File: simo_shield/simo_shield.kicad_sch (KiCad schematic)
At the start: 3 parts, among them U1 YAAJ_BluePill_Part_Like_SWD_B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

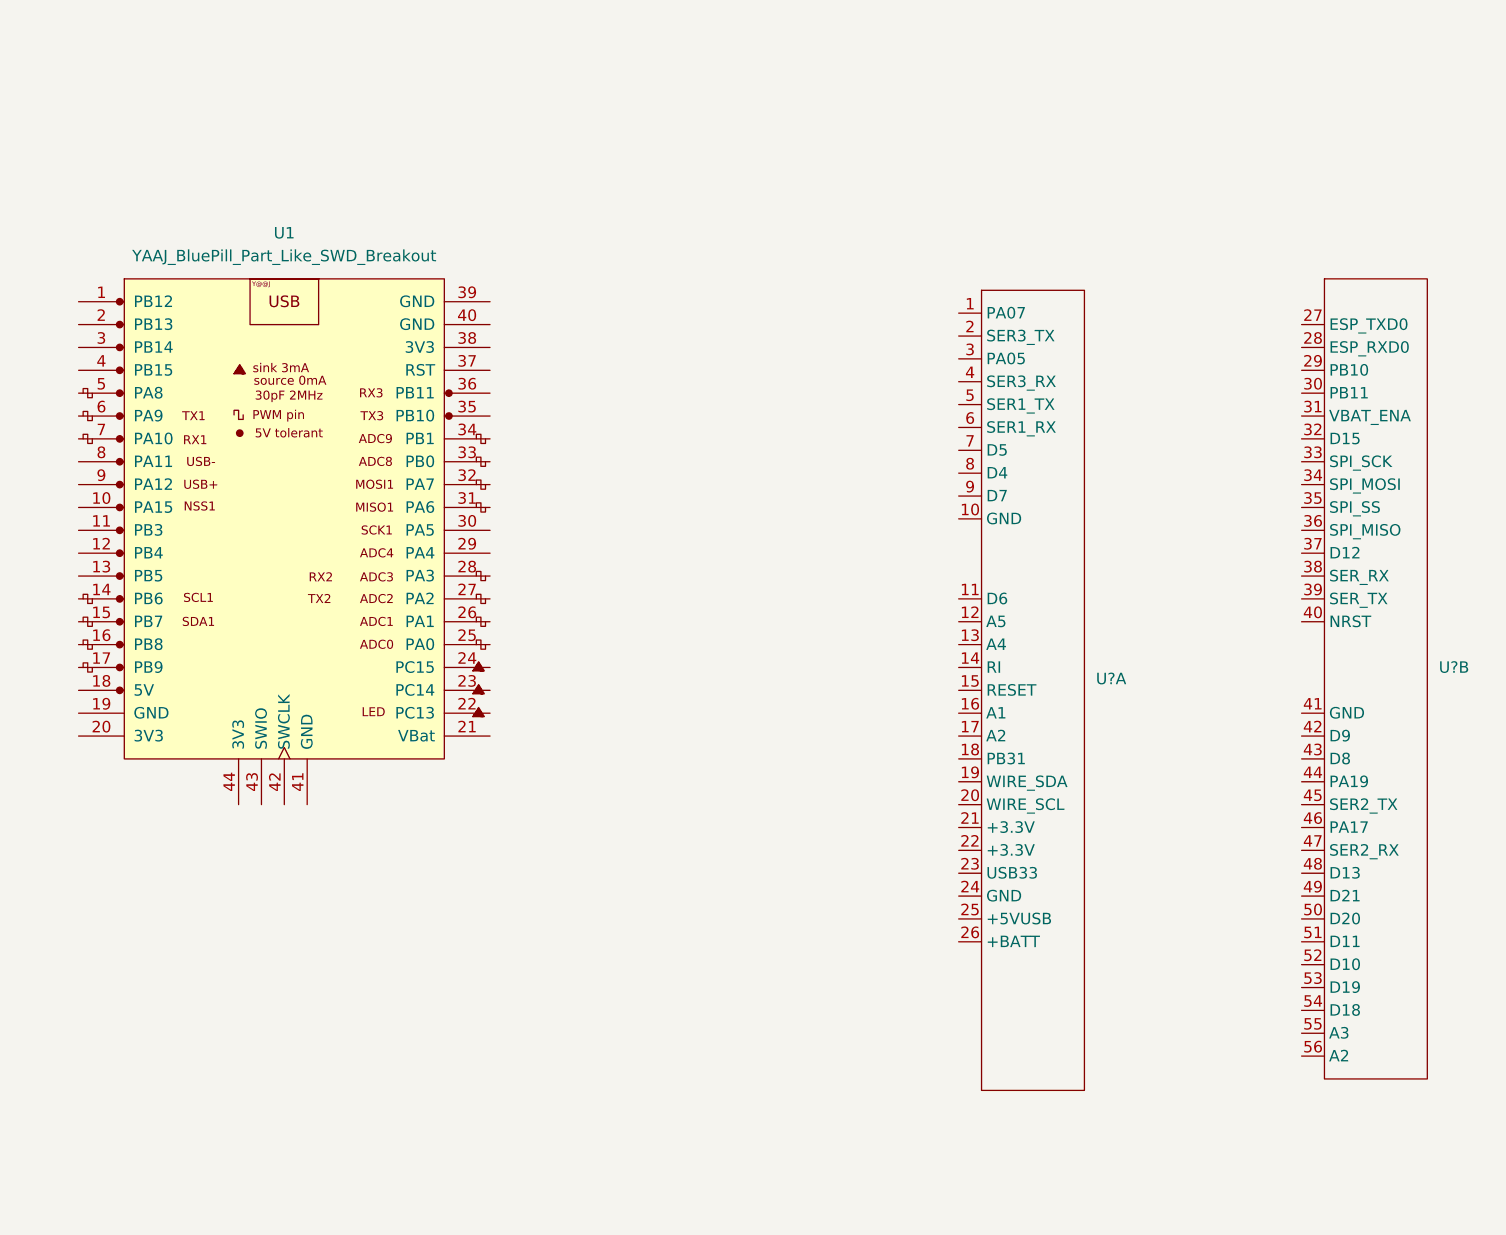
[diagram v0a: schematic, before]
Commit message: organizando proyectos en carpetas: 2 proyectos    , simo_shield (principal) y simo_bateria
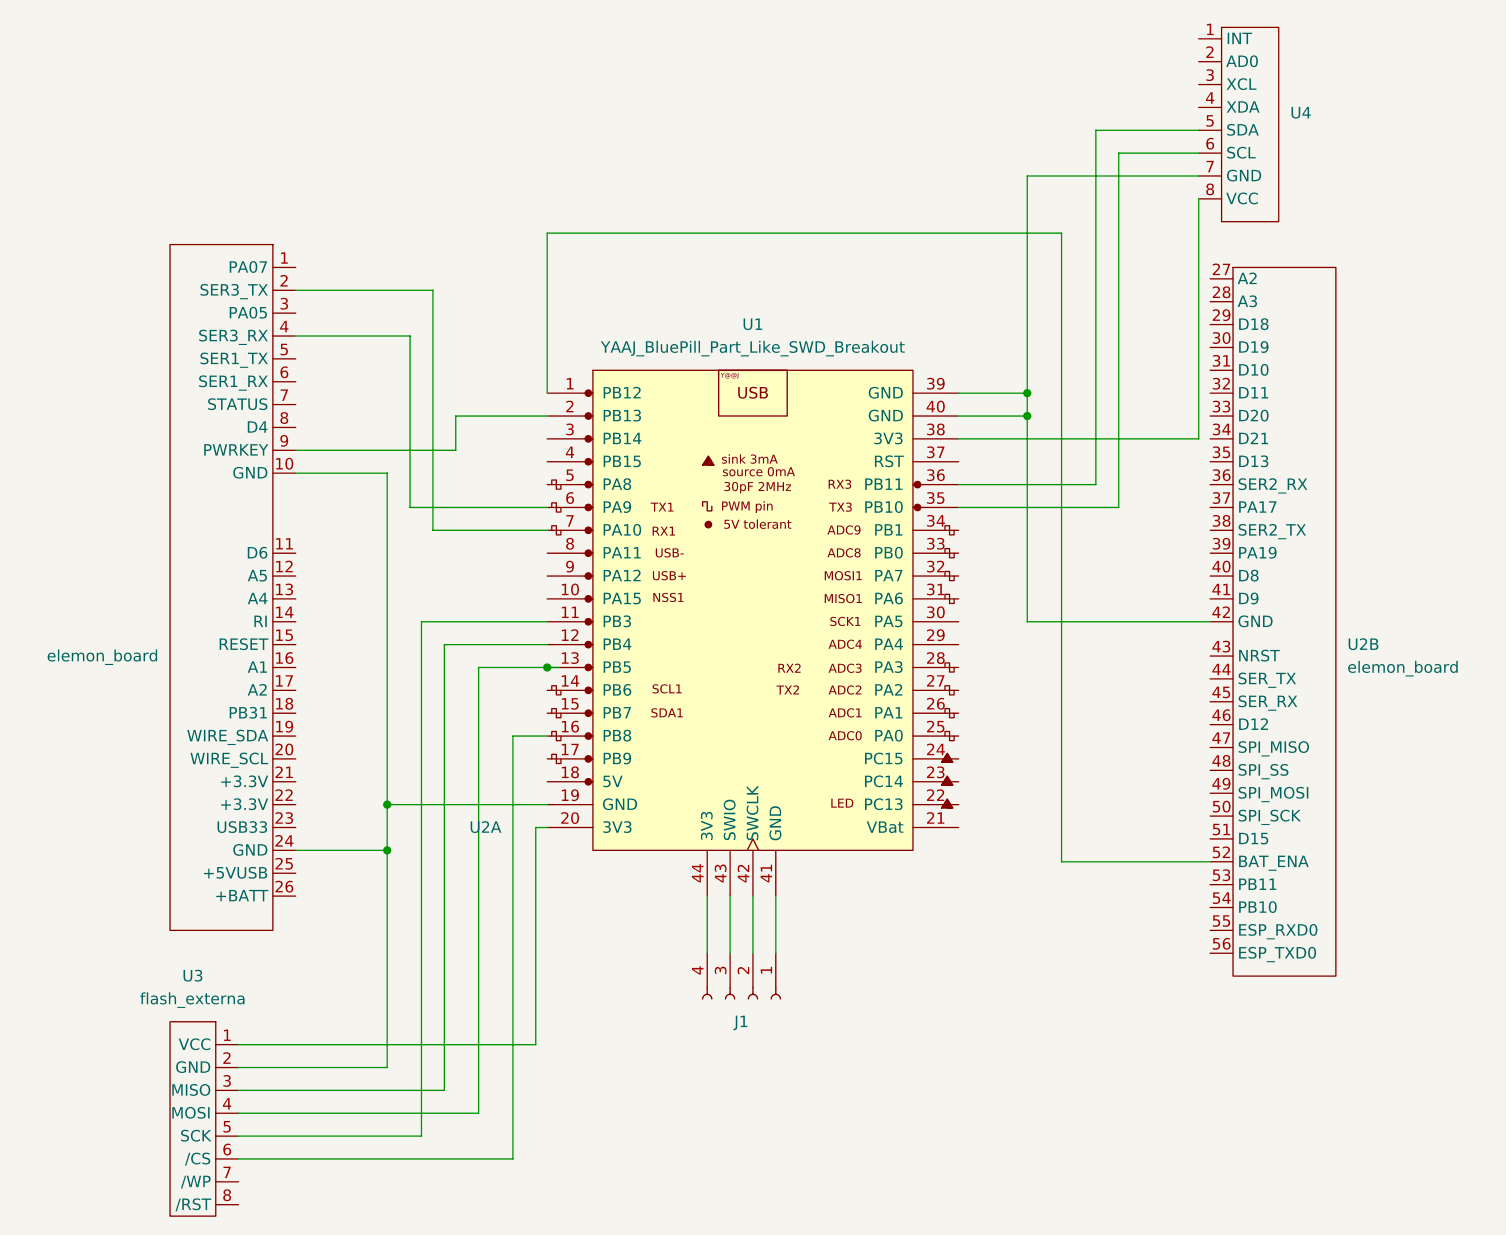
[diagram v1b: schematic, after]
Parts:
- added J1: (no value), symbol Connector:Conn_01x04_Female
- added U3: flash_externa, simo_flash:conector_flash_ext, symbol simo_board:flash_externa
- added U4: (no value), symbol simo_board:mpu6050
- U2: renamed from U?; value (none) -> elemon_board; footprint (none) -> elemon:elemon_board
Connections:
- net at U1.1 (PB12): now also U2.52 (BAT_ENA)
- net at U1.11 (PB3): now also U3.5 (SCK)
- net at U1.12 (PB4): now also U3.3 (MISO)
- net at U1.13 (PB5): now also U3.4 (MOSI)
- net at U1.16 (PB8): now also U3.6 (/CS)
- net at U1.19 (GND): now also U2.10 (GND), U2.24 (GND), U3.2 (GND)
- net at U1.2 (PB13): now also U2.9 (PWRKEY)
- net at U1.20 (3V3): now also U3.1 (VCC)
- net at U1.35 (PB10): now also U4.6 (SCL)
- net at U1.36 (PB11): now also U4.5 (SDA)
- net at U1.38 (3V3): now also U4.8 (VCC)
- net at U1.39 (GND): now also U1.40 (GND), U2.42 (GND), U4.7 (GND)
- net at U1.41 (GND): now also J1.1 (Pin_1)
- net at U1.42 (SWCLK): now also J1.2 (Pin_2)
- net at U1.43 (SWIO): now also J1.3 (Pin_3)
- net at U1.44 (3V3): now also J1.4 (Pin_4)
- net at U1.6 (PA9): now also U2.4 (SER3_RX)
- net at U1.7 (PA10): now also U2.2 (SER3_TX)
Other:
- moved on the sheet: U1, U2A, U2B
